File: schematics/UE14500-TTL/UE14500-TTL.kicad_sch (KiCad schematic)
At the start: 6 parts, among them J1 Edge 1, J2 Edge 2

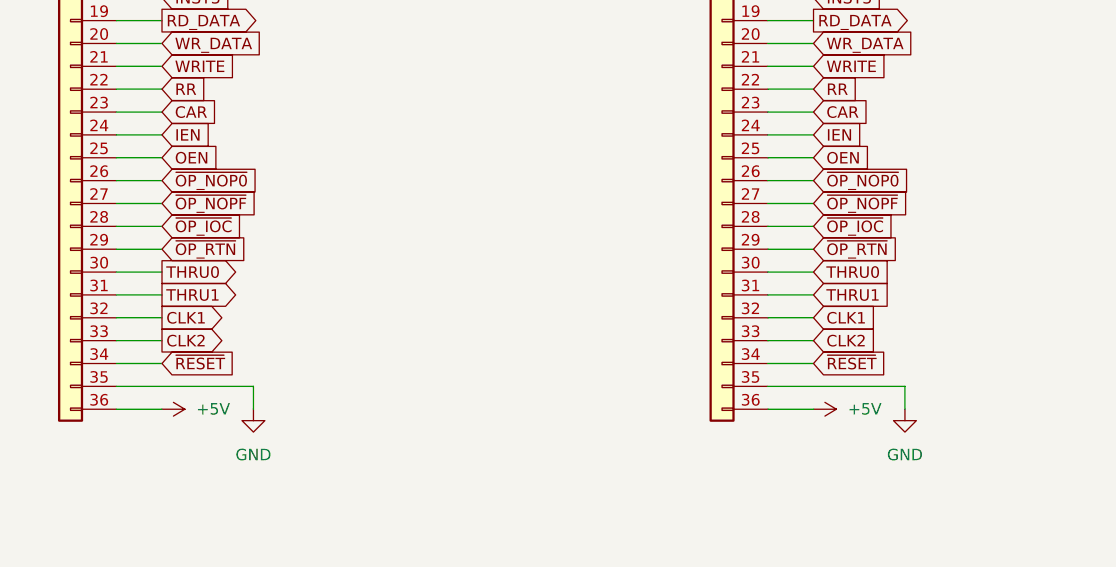
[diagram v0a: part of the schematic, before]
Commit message: Add a tape "REWIND" opcode to reset the PC early
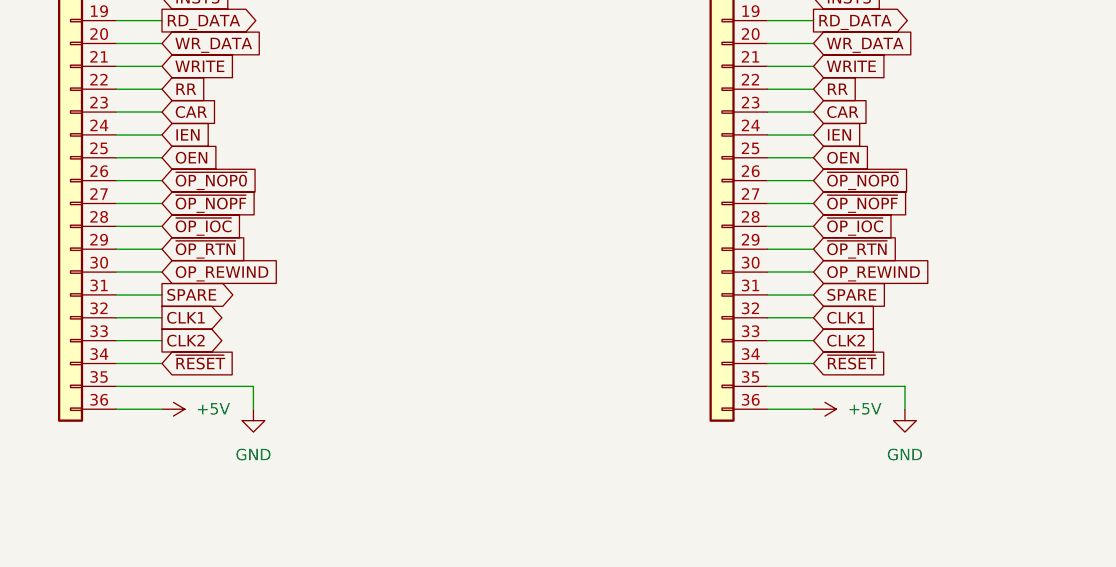
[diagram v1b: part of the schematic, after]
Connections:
- net THRU0 renamed OP_REWIND
- net THRU1 renamed SPARE
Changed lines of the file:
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@@
 		)
 	)
-	(global_label "THRU1"
+	(global_label "SPARE"
 		(shape input)
 		(at 181.61 142.24 0)
@@
 		)
 		(property "Intersheetrefs" "${INTERSHEET_REFS}"
-			(at 190.7033 142.24 0)
+			(at 190.5823 142.24 0)
 			(effects
 				(font
@@
 		)
 	)
-	(global_label "THRU0"
+	(global_label "OP_REWIND"
 		(shape input)
 		(at 181.61 139.7 0)
@@
 		)
 		(property "Intersheetrefs" "${INTERSHEET_REFS}"
-			(at 190.7033 139.7 0)
+			(at 195.239 139.7 0)
 			(effects
 				(font
@@
 		)
 	)
-	(global_label "THRU0"
-		(shape output)
+	(global_label "OP_REWIND"
+		(shape input)
 		(at 109.22 139.7 0)
 		(fields_autoplaced yes)
@@
 		)
 		(property "Intersheetrefs" "${INTERSHEET_REFS}"
-			(at 118.3133 139.7 0)
+			(at 122.849 139.7 0)
 			(effects
 				(font
@@
 		)
 	)
-	(global_label "THRU1"
+	(global_label "SPARE"
 		(shape output)
 		(at 109.22 142.24 0)
@@
 		)
 		(property "Intersheetrefs" "${INTERSHEET_REFS}"
-			(at 118.3133 142.24 0)
-			(effects
-				(font
+			(at 118.1923 142.24 0)
+			(effects
+				(font

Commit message: Make some renderings of the computer
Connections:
- net OP_REWIND renamed REWIND
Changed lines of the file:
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@@
 		)
 	)
-	(global_label "OP_REWIND"
+	(global_label "REWIND"
 		(shape input)
 		(at 181.61 139.7 0)
@@
 		)
 		(property "Intersheetrefs" "${INTERSHEET_REFS}"
-			(at 195.239 139.7 0)
+			(at 191.6709 139.7 0)
 			(effects
 				(font
@@
 		)
 	)
-	(global_label "OP_REWIND"
+	(global_label "REWIND"
 		(shape input)
 		(at 109.22 139.7 0)
@@
 		)
 		(property "Intersheetrefs" "${INTERSHEET_REFS}"
-			(at 122.849 139.7 0)
-			(effects
-				(font
+			(at 119.2809 139.7 0)
+			(effects
+				(font

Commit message: Lay out CPU board
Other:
- note added: "Buffered 4-bit memory address from instruction"
- note added: "Buffered 4-bit opcode from instruction"
- note added: "Carry Register"
- note added: "Clock phase 1"
- note added: "Clock phase 2"
- note added: "D0..D7 - 8-bit instruction fetched from tape, prior to buffering in the 74LS374 flip-flops"
- note added: "Input Enable Register"
- note added: "Low when executing a NOP0 instruction"
- note added: "Low when executing a NOPF instruction"
- note added: "Low when executing a RTN instruction"
- note added: "Low when executing an IOC instruction"
- note added: "Output Enable Register"
- note added: "Read data value in from memory"
- note added: "Reset line"
- note added: "Result Register"
- note added: "Rewind the tape"
- note added: "Spare pass-through pin"
- note added: "Trigger write to memory - latch on falling edge"
- note added: "Write data value out to memory"
- note removed: "Two edge connectors to snap multiple memory and I/O boards to the CPU board."
- moved on the sheet: J1, J2
